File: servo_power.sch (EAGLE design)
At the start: 17 parts, among them T1 2N3904

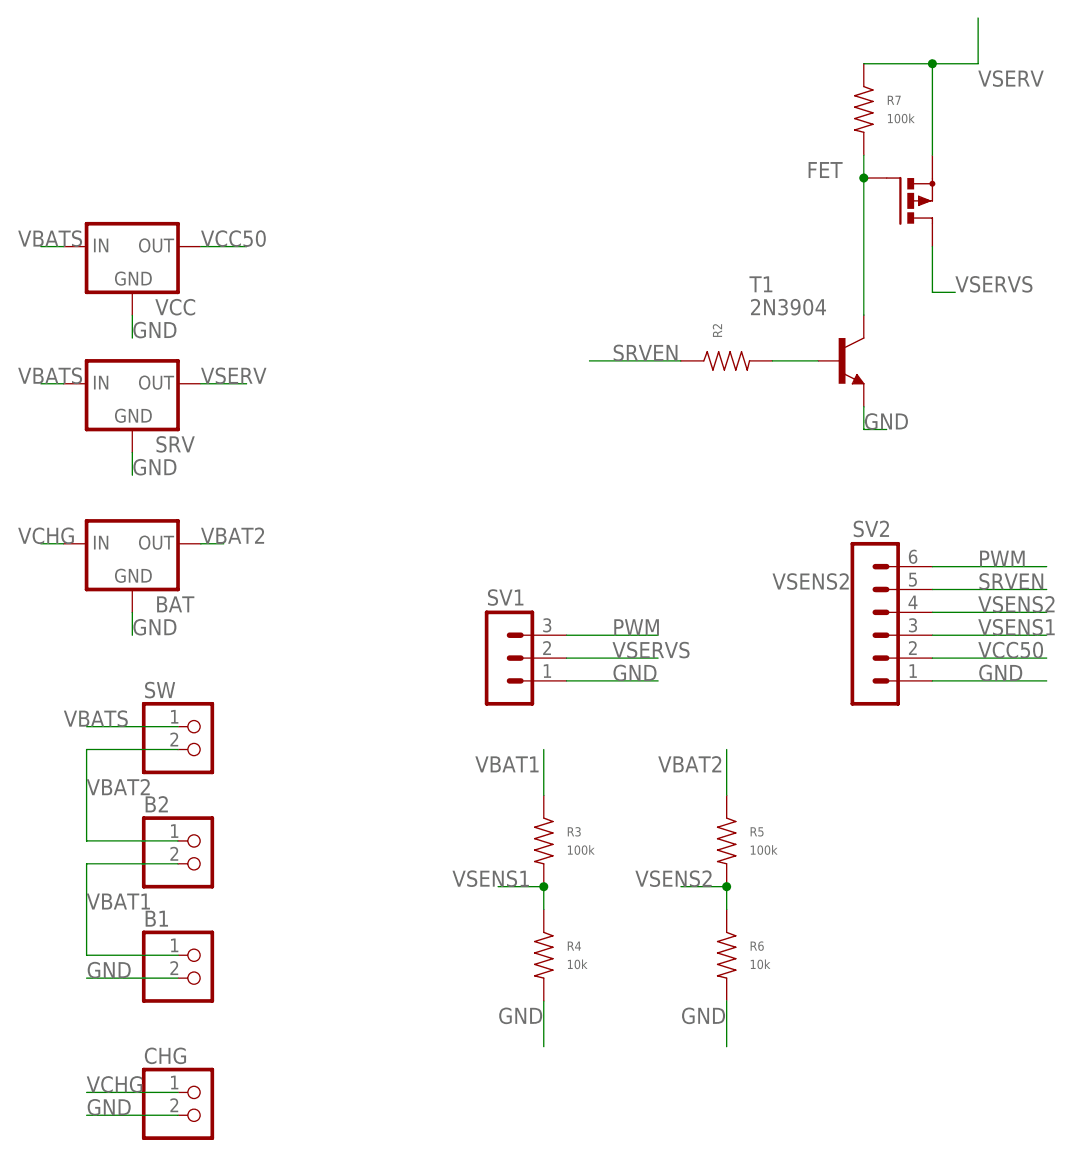
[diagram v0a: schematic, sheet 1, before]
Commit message: PEC11D rotary encoder test chip
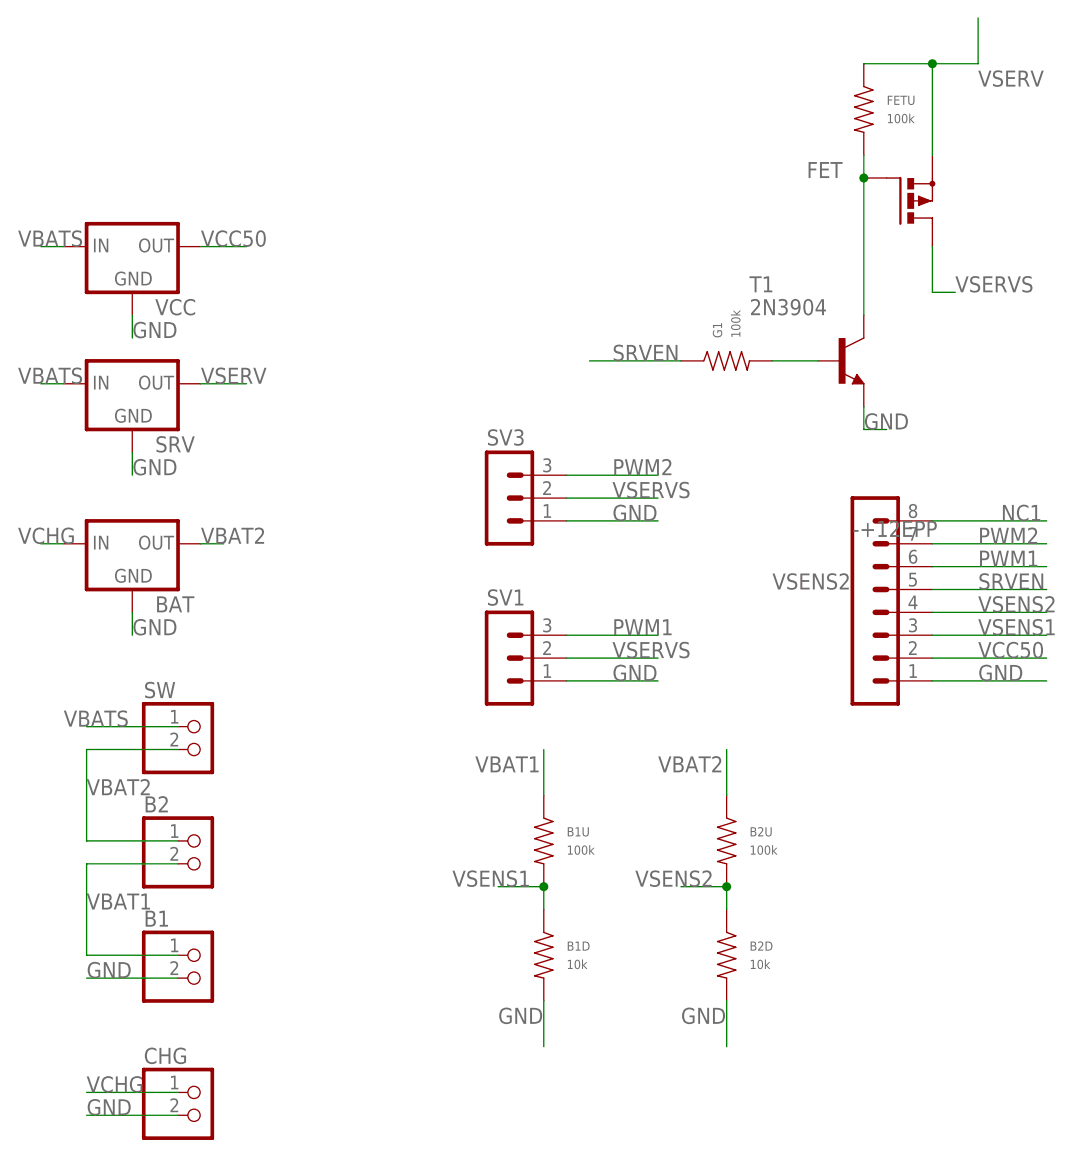
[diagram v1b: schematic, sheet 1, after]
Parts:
- removed SV2: (no value), con-lstb:MA06-1
- added -+12EPP: (no value), con-lstb:MA08-1
- added SV3: (no value), con-lstb:MA03-1
- G1: value (none) -> 100k
- renumbered R2 to G1, R3 to B1U, R4 to B1D, R5 to B2U, R6 to B2D, R7 to FETU
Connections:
- removed net PWM: SV1.3, SV2.6
- new net NC1: -+12EPP.8
- new net PWM1: -+12EPP.6, SV1.3
- new net PWM2: -+12EPP.7, SV3.3
- net GND: now also -+12EPP.1, SV3.1; no longer SV2.1
- net SRVEN: now also -+12EPP.5; no longer SV2.5
- net VCC50: now also -+12EPP.2; no longer SV2.2
- net VSENS1: now also -+12EPP.3; no longer SV2.3
- net VSENS2: now also -+12EPP.4; no longer SV2.4
- net VSERVS: now also SV3.2
